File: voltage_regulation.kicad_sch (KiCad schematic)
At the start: 24 parts, among them IC8 NCV317BD2TR4G, U3 TPS73601DBV, U4 TPS73601DBV

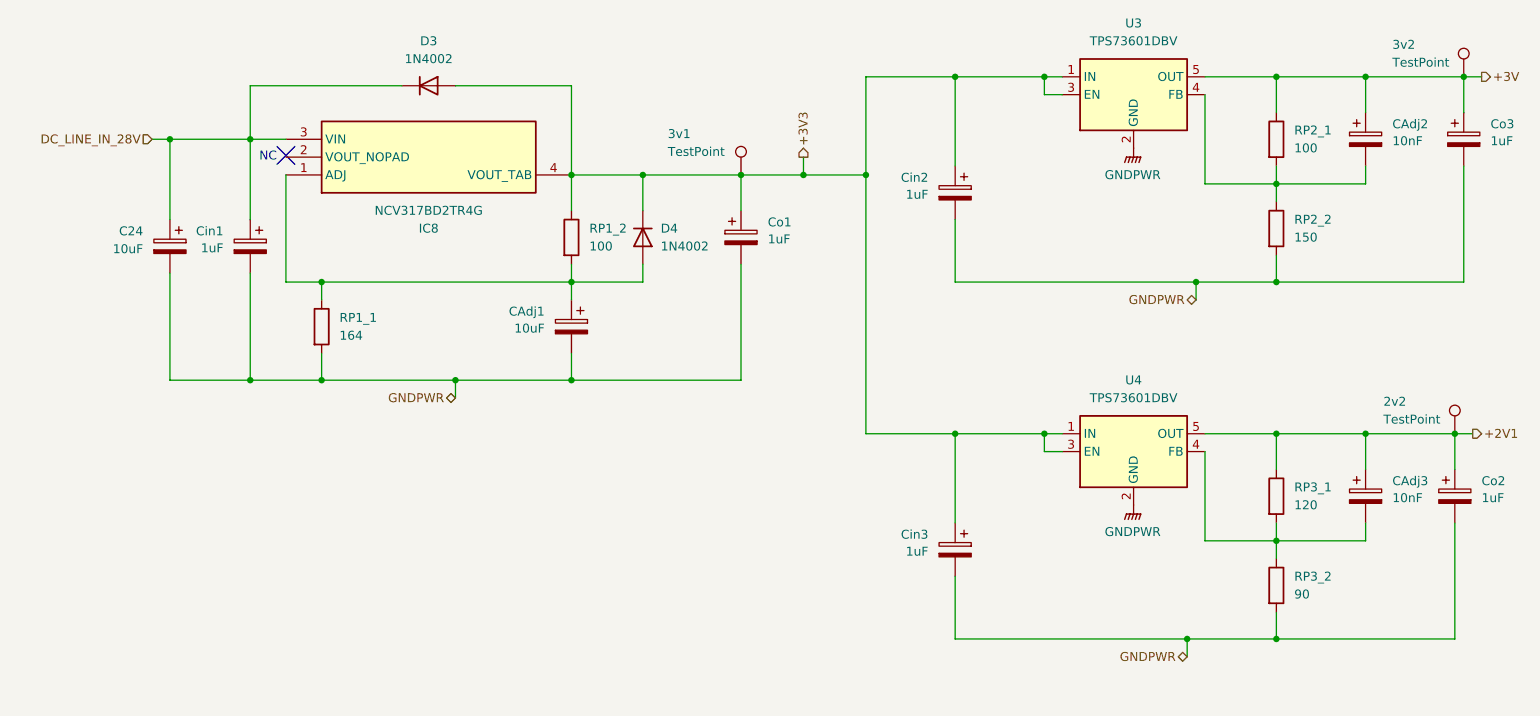
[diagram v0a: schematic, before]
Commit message: One gnd to rule them all; PCB border (90 mm x 90 mm)
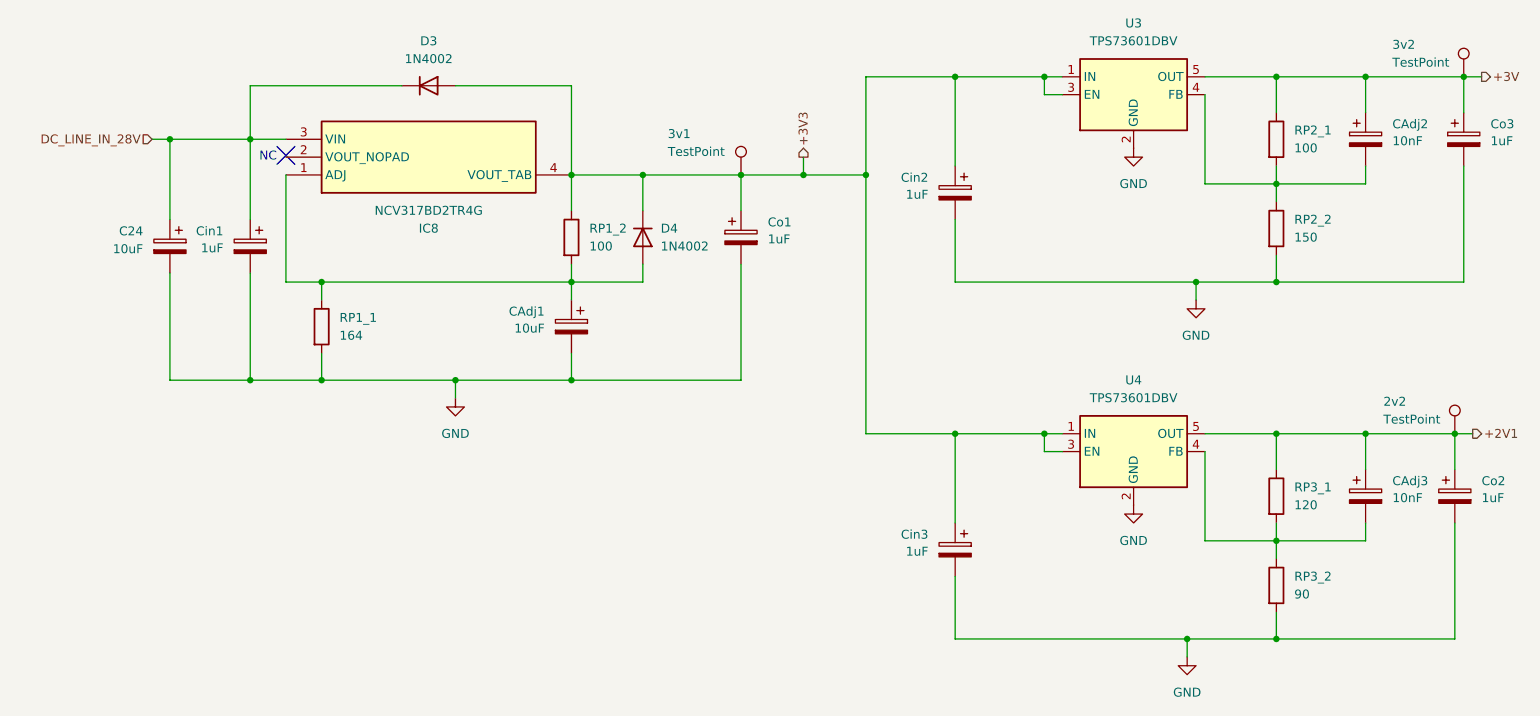
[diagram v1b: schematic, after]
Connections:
- net GNDPWR renamed GND

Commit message: 3v3 Regulator routed; zones for 3v3 and gnd
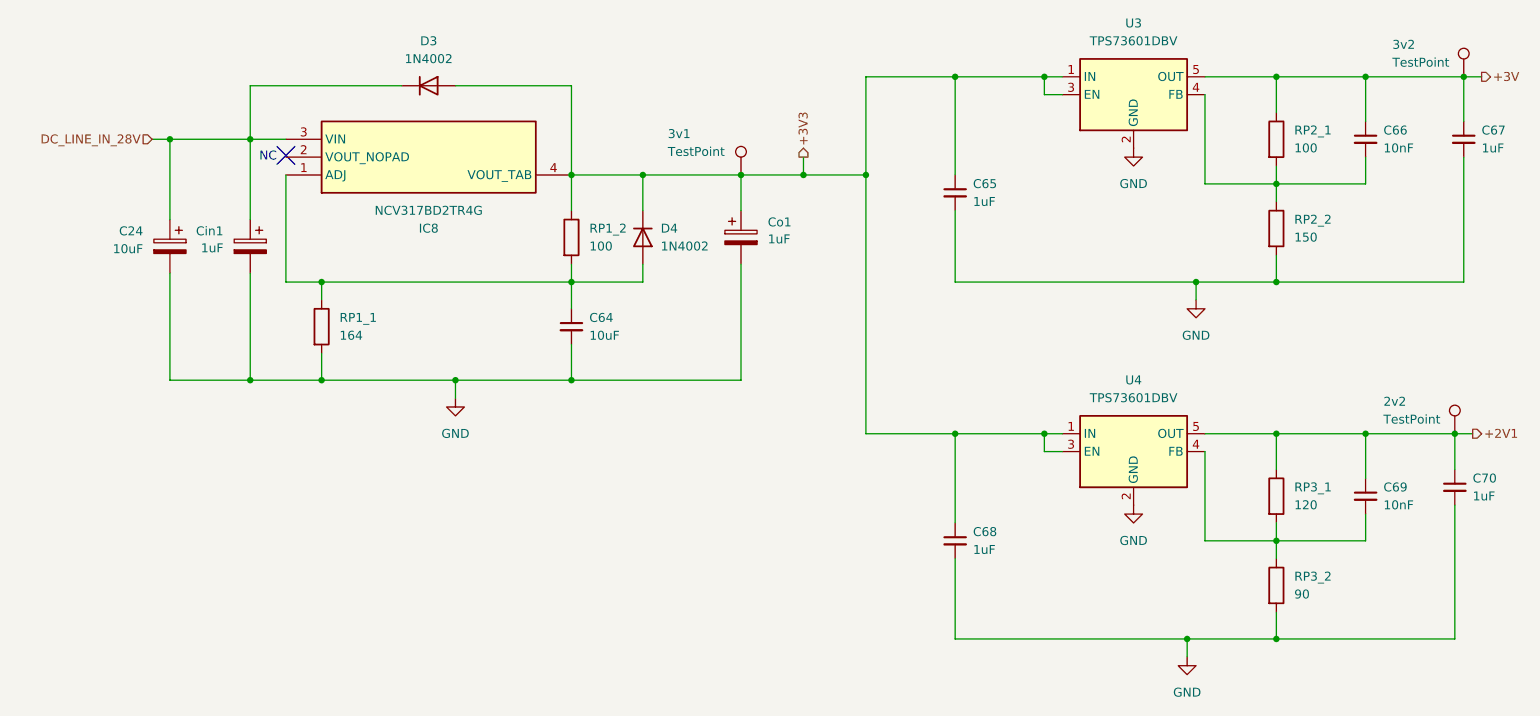
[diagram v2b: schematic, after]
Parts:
- removed CAdj1: 10uF, symbol Device:C_Polarized
- removed CAdj2, CAdj3: 10nF, symbol Device:C_Polarized
- removed Cin2, Cin3, Co2, Co3: 1uF, symbol Device:C_Polarized
- added C64: 10uF, Capacitor_SMD:C_0805_2012Metric, symbol Device:C_Small
- added C65, C67, C68, C70: 1uF, Capacitor_SMD:C_0603_1608Metric, symbol Device:C_Small
- added C66, C69: 10nF, Capacitor_SMD:C_0603_1608Metric, symbol Device:C_Small
- C24: footprint (none) -> Capacitor_SMD:C_0805_2012Metric
- Cin1, Co1, RP1_1: footprint (none) -> Capacitor_SMD:C_0603_1608Metric
- IC8: footprint TO254P1420X457-4N -> SamacSys_Parts:TO254P1420X457-4N
- RP1_2: footprint (none) -> Diode_SMD:D_0603_1608Metric
- RP2_1, RP2_2, RP3_1, RP3_2: footprint (none) -> Resistor_SMD:R_0603_1608Metric
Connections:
- net +2V1: now also C69.1, C70.1
- net +3V: now also C66.1, C67.1
- net +3V3: now also C65.1, C68.1
- net GND: now also C64.2, C65.2, C67.2, C68.2, C70.2
- net at D4.2 (A), IC8.1 (ADJ), RP1_1.1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: now also C64.1
- net at RP3_1.2, RP3_2.1, U4.4 (FB): now also C69.2
- net at RP2_1.2, RP2_2.1, U3.4 (FB): now also C66.2

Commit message: Schematic - Component Specifics
Fixed floating connections.
Added parameters, footprints, Mouser part numbers, and Mouser links to all symbols, including discrete components and ICs.
The following symbols do not have Mouser part numbers or Mouser links:
CMOS Sensor (not required)
RJ45 Connector
JTAG Connector
DC Barrel Jack
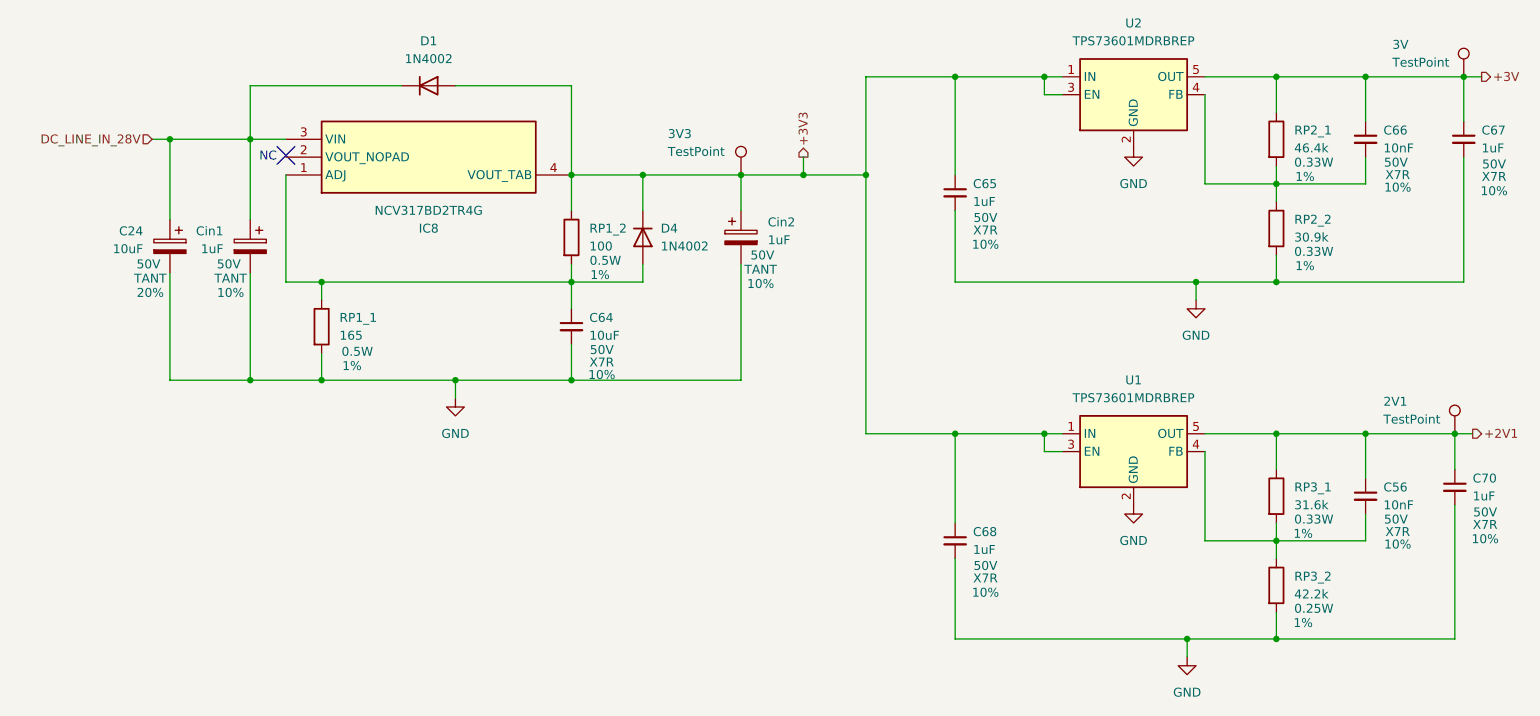
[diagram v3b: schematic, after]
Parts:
- removed C69: 10nF, Capacitor_SMD:C_0603_1608Metric, symbol Device:C_Small
- removed Co1: 1uF, Capacitor_SMD:C_0603_1608Metric, symbol Device:C_Polarized
- removed D3: 1N4002, Diode_THT:D_DO-41_SOD81_P10.16mm_Horizontal, symbol Diode:1N4002
- removed U3, U4: TPS73601DBV, Package_TO_SOT_SMD:SOT-23-5, symbol Regulator_Linear:TPS73601DBV
- added C56: 10nF, Capacitor_SMD:C_0603_1608Metric, symbol Device:C_Small
- added Cin2: 1uF, Capacitor_SMD:C_1206_3216Metric, symbol Device:C_Polarized
- added D1: 1N4002, Diode_THT:D_DO-41_SOD81_P10.16mm_Horizontal, symbol Diode:1N4002
- added U1, U2: TPS73601MDRBREP, Package_TO_SOT_SMD:SOT-23-5, symbol Regulator_Linear:TPS73601DBV
- C24: footprint Capacitor_SMD:C_0805_2012Metric -> Capacitor_Tantalum_SMD:CP_EIA-7343-31_Kemet-D; Dielectric (none) -> TANT; Mouser Part Number (none) -> 80-T598D106M050ATS90; Mouser Price/Stock (none) -> https://www.mouser.com/ProductDetail/KEMET/T598D106M050ATS0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; Tolerance (none) -> 20%; Voltage Rating (none) -> 50V
- C64: footprint Capacitor_SMD:C_0805_2012Metric -> Capacitor_SMD:C_1206_3216Metric; Dielectric (none) -> X7R; Mouser Part Number (none) -> 187-CL31B106KBK6PJE; Mouser Price/Stock (none) -> https://www.mouser.com/ProductDetail/Samsung-Electro-Mechan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; Tolerance (none) -> 10%; Voltage Rating (none) -> 50V
- C65, C67, C68, C70: Dielectric (none) -> X7R; Mouser Part Number (none) -> 963-MLASU168AB7105KT; Mouser Price/Stock (none) -> https://www.mouser.com/ProductDetail/TAIYO-YUDEN/MLASU168AB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; Tolerance (none) -> 10%; Voltage Rating (none) -> 50V
- C66: Dielectric (none) -> X7R; Mouser Part Number (none) -> 81-GCM188R71H103KA7J; Mouser Price/Stock (none) -> https://www.mouser.com/ProductDetail/Murata-Electronics/GCM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; Tolerance (none) -> 10%; Voltage Rating (none) -> 50V
- Cin1: footprint Capacitor_SMD:C_0603_1608Metric -> Capacitor_SMD:C_1206_3216Metric; Dielectric (none) -> TANT; Mouser Part Number (none) -> 80-T491A105K050AT; Mouser Price/Stock (none) -> https://www.mouser.com/ProductDetail/KEMET/T491A105K050AT?q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; Tolerance (none) -> 10%; Voltage Rating (none) -> 50V
- D4: Mouser Part Number (none) -> 637-1N4002; Mouser Price/Stock (none) -> https://www.mouser.com/ProductDetail/Diotec-Semiconductor/1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
- IC8: Arrow Part Number NCV317BD2TR4G -> (none); Arrow Price/Stock https://www.arrow.com/en/products/ncv317bd2tr4g/on-semicond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 -> (none); Mouser Part Number (none) -> 863-NCV317BD2TR4G; Mouser Price/Stock (none) -> https://www.mouser.com/ProductDetail/onsemi/NCV317BD2TR4G?q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
- RP1_1: value 164 -> 165; footprint Capacitor_SMD:C_0603_1608Metric -> Resistor_SMD:R_0805_2012Metric; Mouser Part Number (none) -> 667-ERJ-UP6F1650V; Mouser Price/Stock (none) -> https://www.mouser.com/ProductDetail/Panasonic/ERJ-UP6F1650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; Power Rating (none) -> 0.5W; Tolerance (none) -> 1%
- RP1_2: footprint Diode_SMD:D_0603_1608Metric -> Resistor_SMD:R_0805_2012Metric; Mouser Part Number (none) -> 71-CRCW0805100RFKEAH; Mouser Price/Stock (none) -> https://www.mouser.com/ProductDetail/Vishay-Dale/CRCW080510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; Power (none) -> 0.5W; Tolerance (none) -> 1%
- RP2_1: value 100 -> 46.4k; Mouser Part Number (none) -> 71-CRCW060346K4FKEAH; Mouser Price/Stock (none) -> https://www.mouser.com/ProductDetail/Vishay-Dale/CRCW060346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; Power Rating (none) -> 0.33W; Tolerance (none) -> 1%
- RP2_2: value 150 -> 30.9k; Mouser Part Number (none) -> 71-CRCW060330K9FKEAH; Mouser Price/Stock (none) -> https://www.mouser.com/ProductDetail/Vishay-Dale/CRCW060330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; Power Rating (none) -> 0.33W; Tolerance (none) -> 1%
- RP3_1: value 120 -> 31.6k; Mouser Part Number (none) -> 71-CRCW060331K6FKEAH; Mouser Price/Stock (none) -> https://www.mouser.com/ProductDetail/Vishay-Dale/CRCW060331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; Power Rating (none) -> 0.33W; Tolerance (none) -> 1%
- RP3_2: value 90 -> 42.2k; Mouser Part Number (none) -> 71-RCS060342K2FKEA; Mouser Price/Stock (none) -> https://www.mouser.com/ProductDetail/Vishay-Dale/RCS060342K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; Power Rating (none) -> 0.25W; Tolerance (none) -> 1%
- renumbered 2v2 to 2V1, 3v2 to 3V, 3v1 to 3V3
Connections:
- net +2V1: now also C56.1, U1.5 (OUT)
- net +3V: now also U2.5 (OUT)
- net +3V3: now also Cin2.1, D1.2 (A), U1.1 (IN), U1.3 (EN), U2.1 (IN), U2.3 (EN)
- net DC_LINE_IN_28V: now also D1.1 (K)
- net GND: now also Cin2.2, U1.2 (GND), U2.2 (GND)
- net at RP3_1.2, RP3_2.1: now also C56.2, U1.4 (FB)
- net at C66.2, RP2_1.2, RP2_2.1: now also U2.4 (FB)

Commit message: Some small changes for BOM
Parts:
- 2V1, 3V, 3V3: now left out of the parts list
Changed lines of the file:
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@@
 		(unit 1)
 		(exclude_from_sim no)
-		(in_bom yes)
+		(in_bom no)
 		(on_board yes)
 		(dnp no)
@@
 		(unit 1)
 		(exclude_from_sim no)
-		(in_bom yes)
+		(in_bom no)
 		(on_board yes)
 		(dnp no)
@@
 		(unit 1)
 		(exclude_from_sim no)
-		(in_bom yes)
-		(on_board yes)
-		(dnp no)
+		(in_bom no)
+		(on_board yes)
+		(dnp no)
